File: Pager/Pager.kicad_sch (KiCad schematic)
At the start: 18 parts, among them U1 ESP32-S3-MINI-1, Y1 ABS25-32.768KHZ-6-T

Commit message: brh
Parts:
- added F1: Fuse_Small, symbol Device:Fuse_Small
- added J2: Conn_01x02_Pin, symbol Connector:Conn_01x02_Pin
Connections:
- net Batt_Sense+: now reaches U1.6 (IO2)
- net Charging: now reaches U1.7 (IO3)
- net USBD+ renamed Power/USBD+
- net USBD- renamed Power/USBD-
- new net Battery+: F1.2
- new net Battery-: J2.2 (Pin_2)
- new net V_{BATT}: F1.1, J2.1 (Pin_1)
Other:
- added sheet Buttons (buttons.kicad_sch)
- added sheet Buzzer (buzzer.kicad_sch)
- added sheet Screen (screen.kicad_sch)
- sheet Power ports: added Batt_Sense+, Charging, USBD+, USBD-; removed none
- note added: "Battery Connector"

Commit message: br
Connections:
- net Buttons/Button_3: now reaches U1.10 (IO6)
- net Buttons/Button_4: now reaches U1.11 (IO7)
- net Buttons/Button_5: now reaches U1.12 (IO8)
- net Buttons/Button_1: now reaches U1.8 (IO4)
- net Buttons/Button_2: now reaches U1.9 (IO5)
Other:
- sheet Buttons ports: added Button_1, Button_2, Button_3, Button_4, Button_5; removed none

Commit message: br
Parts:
- added J3: Conn_01x04_Pin, Package_DFN_QFN:QFN-20-1EP_5x5mm_P0.65mm_EP3.35x3.35mm, symbol Connector:Conn_01x04_Pin
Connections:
- net +3V3: now also J3.3 (Pin_3)
- net Buttons/Button_5: now also U1.15 (IO11); no longer U1.12 (IO8)
- net GND: now also J3.4 (Pin_4)
- net SDA: now reaches U1.13 (IO9)
- net SDA: now also J3.2 (Pin_2)
- new net SCK: J3.1 (Pin_1), U1.12 (IO8)
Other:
- removed sheet Screen

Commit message: br
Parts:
- added C19: C_Small, Package_SO:SOIC-16_3.9x9.9mm_P1.27mm, symbol Device:C_Small
- added R21: R_Small, Resistor_THT:R_Array_SIP4, symbol Device:R_Small
- added R22: 20k, Resistor_THT:R_Array_SIP4, symbol Device:R_Small
- added R23: 10k, Resistor_THT:R_Array_SIP4, symbol Device:R_Small
- added R24, R25: 4.7k, Resistor_THT:R_Array_SIP4, symbol Device:R_Small
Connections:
- net Battery+ is gone; now on net V_{BATT}: F1.2
- net Battery- is gone; now on net GND: J2.2 (Pin_2)
- net +3V3: now also C19.1, R21.1, R24.1, R25.1
- net Charging: now also R22.1; no longer U1.7 (IO3)
- net GND: now also C19.2, R23.2
- net SCK: now also R24.2
- net SDA: now also R25.2
- net V_{BATT}: no longer F1.1, J2.1 (Pin_1)
- net at U1.22 (IO18): now also R22.2, R23.1
- net at U1.45 (EN): now also R21.2
- net Buzzer/BUZZER_PWM: now reaches U1.5 (IO1)
- new net: F1.1, J2.1 (Pin_1)
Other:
- sheet Buzzer ports: added BUZZER_PWM; removed none

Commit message: connected radio to mcu
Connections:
- net RF_SI: now reaches U1.31 (IO35)
- net RF_SCLK: now reaches U1.32 (IO36)
- net RF_SO: now reaches U1.33 (IO37)
- net RF_CSn: now reaches U1.35 (IO39)
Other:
- sheet Radio ports: added RF_CSn, RF_GDO0, RF_GDO1, RF_GDO2, RF_SCLK, RF_SI; removed none

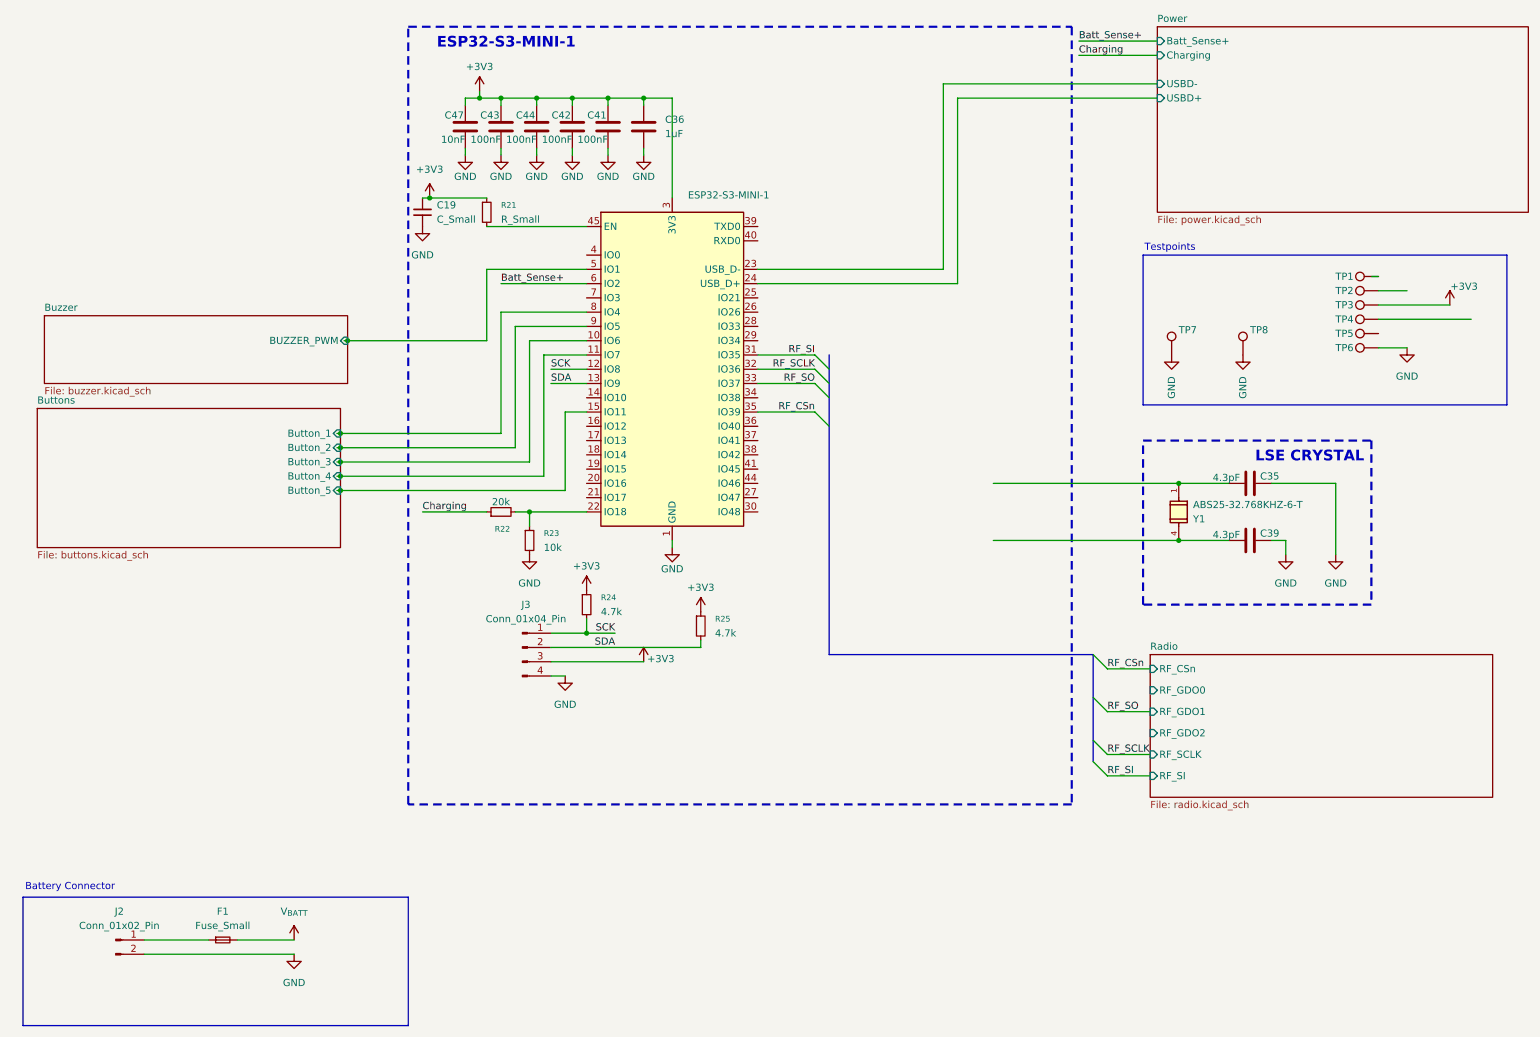
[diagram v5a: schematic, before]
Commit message: Schematic Review, Footprints Added, Need Screen
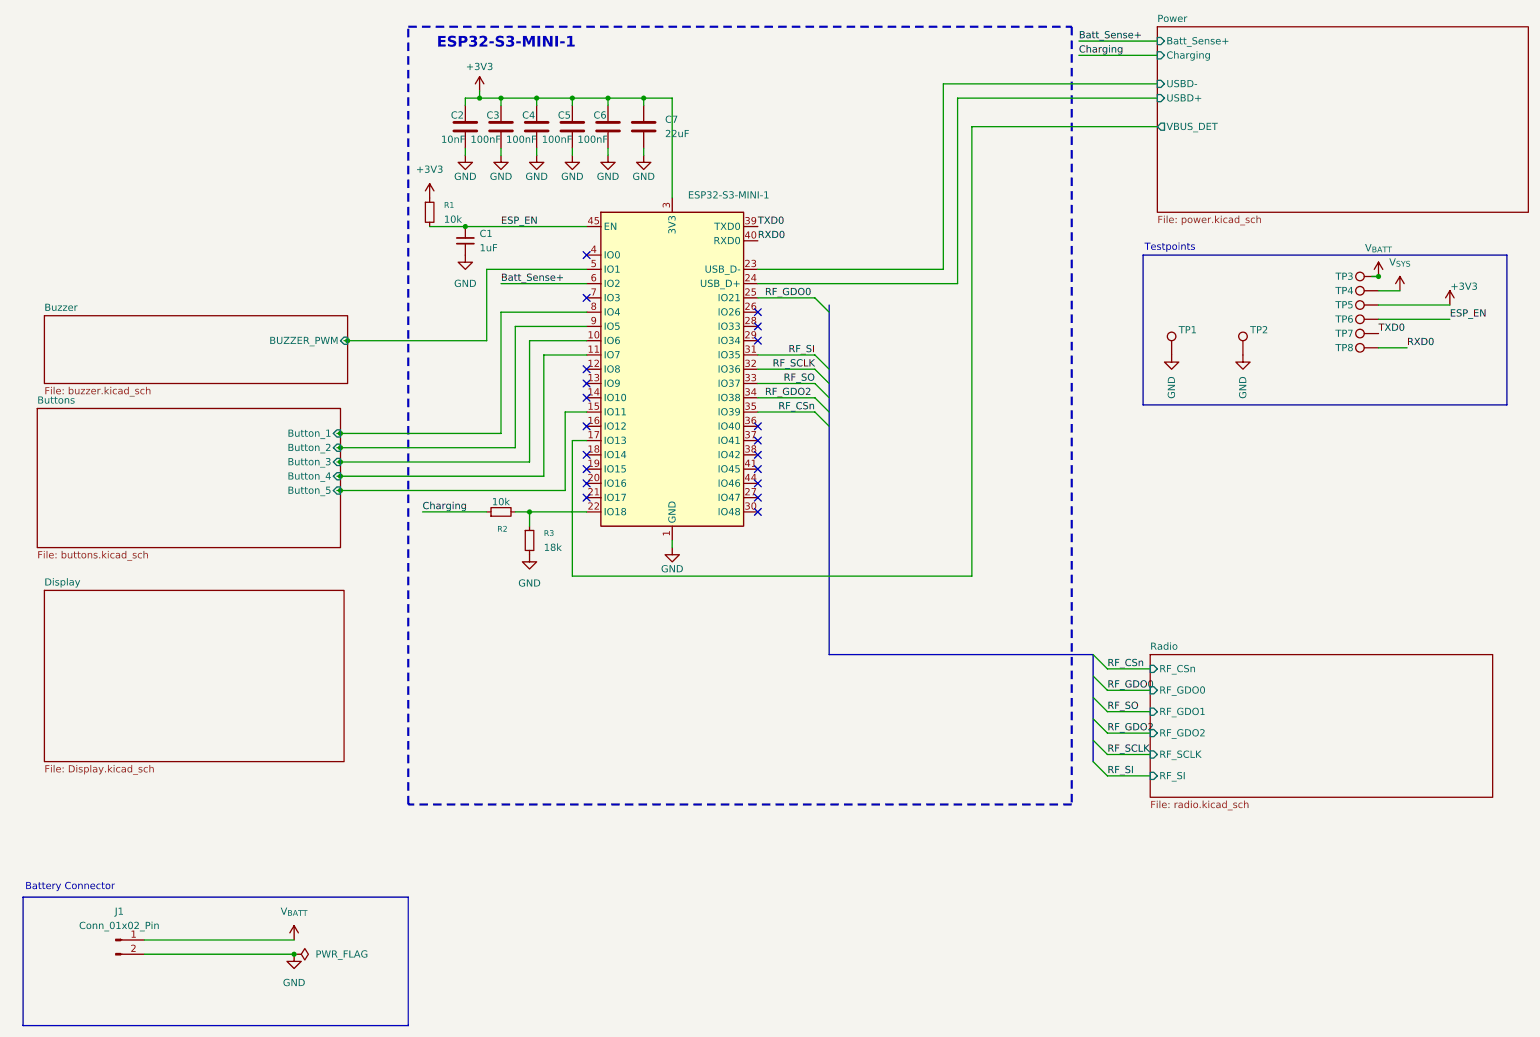
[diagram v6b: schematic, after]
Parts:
- removed C35, C39: 4.3pF, Capacitor_SMD:C_0603_1608Metric, symbol Device:C
- removed F1: Fuse_Small, symbol Device:Fuse_Small
- removed J3: Conn_01x04_Pin, Package_DFN_QFN:QFN-20-1EP_5x5mm_P0.65mm_EP3.35x3.35mm, symbol Connector:Conn_01x04_Pin
- removed R24, R25: 4.7k, Resistor_THT:R_Array_SIP4, symbol Device:R_Small
- removed Y1: ABS25-32.768KHZ-6-T, Crystal:Crystal_SMD_Abracon_ABS25-4Pin_8.0x3.8mm, symbol ABS25-32.768KHZ-6-T:ABS25-32.768KHZ-6-T
- C1: renamed from C19; value C_Small -> 1uF; footprint Package_SO:SOIC-16_3.9x9.9mm_P1.27mm -> Capacitor_SMD:C_0603_1608Metric
- C7: renamed from C36; value 1uF -> 22uF; footprint Capacitor_SMD:C_0603_1608Metric -> Capacitor_SMD:C_0805_2012Metric
- J1: renamed from J2; footprint (none) -> Connector_JST:JST_PH_S2B-PH-SM4-TB_1x02-1MP_P2.00mm_Horizontal
- R1: renamed from R21; value R_Small -> 10k; footprint Resistor_THT:R_Array_SIP4 -> Package_TO_SOT_SMD:SOT-23
- R2: renamed from R22; value 20k -> 10k; footprint Resistor_THT:R_Array_SIP4 -> Package_TO_SOT_SMD:SOT-23
- R3: renamed from R23; value 10k -> 18k; footprint Resistor_THT:R_Array_SIP4 -> Package_TO_SOT_SMD:SOT-23
- renumbered C47 to C2, C43 to C3, C44 to C4, C42 to C5, C41 to C6, TP7 to TP1, TP8 to TP2, TP1 to TP3, TP2 to TP4, TP3 to TP5, TP4 to TP6, TP5 to TP7, TP6 to TP8
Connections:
- net +3V3: no longer C1.1
- net GND: no longer TP8.1
- net V_{BATT}: now also J1.1 (Pin_1), TP3.1
- net Power/VBUS_DET: now reaches U1.17 (IO13)
- net at U1.25 (IO21): no longer names the net of U1.25 (IO21)
- net RF_GDO2: now reaches U1.34 (IO38)
- net TXD0: now reaches U1.39 (TXD0)
- net TXD0: now also TP7.1
- net RXD0: now reaches U1.40 (RXD0)
- net RXD0: now also TP8.1
- net ESP_EN: now reaches R1.2, U1.45 (EN)
- net ESP_EN: now also C1.1, TP6.1
- net V_{SYS}: now reaches TP4.1
- net SCK: no longer names the net of U1.12 (IO8)
- net SDA: no longer names the net of U1.13 (IO9)
- no-connect marks 0 -> 20
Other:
- added sheet Display (Display.kicad_sch)
- sheet Power ports: added VBUS_DET; removed none
- note removed: "LSE CRYSTAL"
- moved on the sheet: C1, R1

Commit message: layout
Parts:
- C1, C2, C3, C4, C5, C6: footprint Capacitor_SMD:C_0603_1608Metric -> Capacitor_SMD:C_0805_2012Metric_Pad1.18x1.45mm_HandSolder
- C7: footprint Capacitor_SMD:C_0805_2012Metric -> Capacitor_SMD:C_0805_2012Metric_Pad1.18x1.45mm_HandSolder
- R1, R2, R3: footprint Package_TO_SOT_SMD:SOT-23 -> Resistor_SMD:R_0805_2012Metric_Pad1.20x1.40mm_HandSolder
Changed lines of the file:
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@@
 			)
 		)
-		(property "Footprint" "Capacitor_SMD:C_0603_1608Metric"
+		(property "Footprint" "Capacitor_SMD:C_0805_2012Metric_Pad1.18x1.45mm_HandSolder"
 			(at 93.0148 39.37 0)
 			(hide yes)
@@
 			)
 		)
-		(property "Footprint" "Package_TO_SOT_SMD:SOT-23"
+		(property "Footprint" "Resistor_SMD:R_0805_2012Metric_Pad1.20x1.40mm_HandSolder"
 			(at 100.33 104.14 0)
 			(hide yes)
@@
 			)
 		)
-		(property "Footprint" "Capacitor_SMD:C_0603_1608Metric"
+		(property "Footprint" "Capacitor_SMD:C_0805_2012Metric_Pad1.18x1.45mm_HandSolder"
 			(at 112.0648 39.37 0)
 			(hide yes)
@@
 			)
 		)
-		(property "Footprint" "Capacitor_SMD:C_0603_1608Metric"
+		(property "Footprint" "Capacitor_SMD:C_0805_2012Metric_Pad1.18x1.45mm_HandSolder"
 			(at 99.3648 39.37 0)
 			(hide yes)
@@
 			)
 		)
-		(property "Footprint" "Capacitor_SMD:C_0603_1608Metric"
+		(property "Footprint" "Capacitor_SMD:C_0805_2012Metric_Pad1.18x1.45mm_HandSolder"
 			(at 118.4148 39.37 0)
 			(hide yes)
@@
 			)
 		)
-		(property "Footprint" "Package_TO_SOT_SMD:SOT-23"
+		(property "Footprint" "Resistor_SMD:R_0805_2012Metric_Pad1.20x1.40mm_HandSolder"
 			(at 105.41 109.22 0)
 			(hide yes)
@@
 			)
 		)
-		(property "Footprint" "Capacitor_SMD:C_0603_1608Metric"
+		(property "Footprint" "Capacitor_SMD:C_0805_2012Metric_Pad1.18x1.45mm_HandSolder"
 			(at 105.7148 39.37 0)
 			(hide yes)
@@
 			)
 		)
-		(property "Footprint" "Capacitor_SMD:C_0603_1608Metric"
+		(property "Footprint" "Capacitor_SMD:C_0805_2012Metric_Pad1.18x1.45mm_HandSolder"
 			(at 93.98 55.88 0)
 			(hide yes)
@@
 			)
 		)
-		(property "Footprint" "Package_TO_SOT_SMD:SOT-23"
+		(property "Footprint" "Resistor_SMD:R_0805_2012Metric_Pad1.20x1.40mm_HandSolder"
 			(at 87.63 50.8 0)
 			(hide yes)
@@
 			)
 		)
-		(property "Footprint" "Capacitor_SMD:C_0805_2012Metric"
+		(property "Footprint" "Capacitor_SMD:C_0805_2012Metric_Pad1.18x1.45mm_HandSolder"
 			(at 126.6952 39.37 0)
 			(hide yes)

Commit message: esp32
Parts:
- added C34, C35: 100nF, Capacitor_SMD:C_0603_1608Metric, symbol Device:C_Small
- added R32, R42: 10k, Resistor_SMD:R_0603_1608Metric, symbol Device:R_Small
- added R39, R43: 1k, Resistor_SMD:R_0603_1608Metric, symbol Device:R_Small
- added SW7, SW8: SW_Push, Button_Switch_SMD:SW_SPST_TL3342, symbol Switch:SW_Push
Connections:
- net +3V3: now also R32.1, R42.1
- net Batt_Sense+: now also U1.13 (IO9); no longer U1.6 (IO2)
- net GND: now also C34.2, C35.2, SW7.2, SW8.2
- net Buzzer_PWM: now reaches U1.14 (IO10)
- net Button_6: now reaches U1.4 (IO0)
- net Button_6: now also C34.1, R39.2
- net Buzzer/BUZZER_PWM renamed Button_7
- net Button_7: now also C35.1, R43.2
- new net: R42.2, R43.1, SW8.1
- new net: R32.2, R39.1, SW7.1
- no-connect marks 20 -> 17
